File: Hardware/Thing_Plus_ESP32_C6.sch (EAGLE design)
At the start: 48 parts, among them J1 THING_PLUS_LOGICAL, J4 QWIIC_RIGHT_ANGLE, J5 MICRO-SDFRICTION, Q1 20V/4.2A/52mΩ/1.4W, U1 ESP32-C6-WROOM-1-NARROW, U2 RT9080-33GJ5, U3 MCP73831, U4 MAX17048

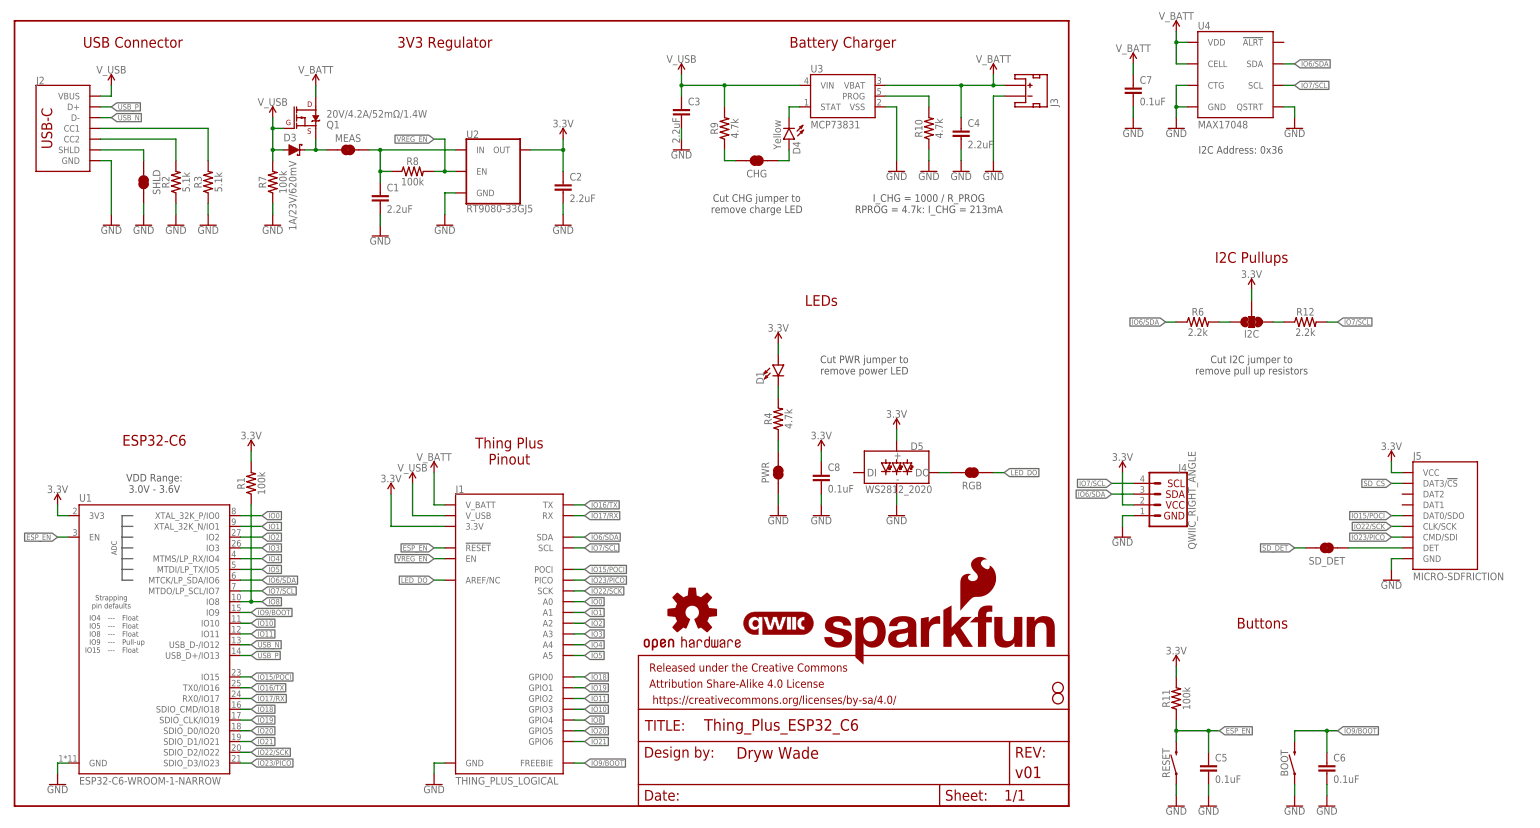
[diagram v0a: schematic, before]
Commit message: Finish initial schematic and layout
Organized schematic
Rearranged power circuitry to make routing other components easier
Finished routing board
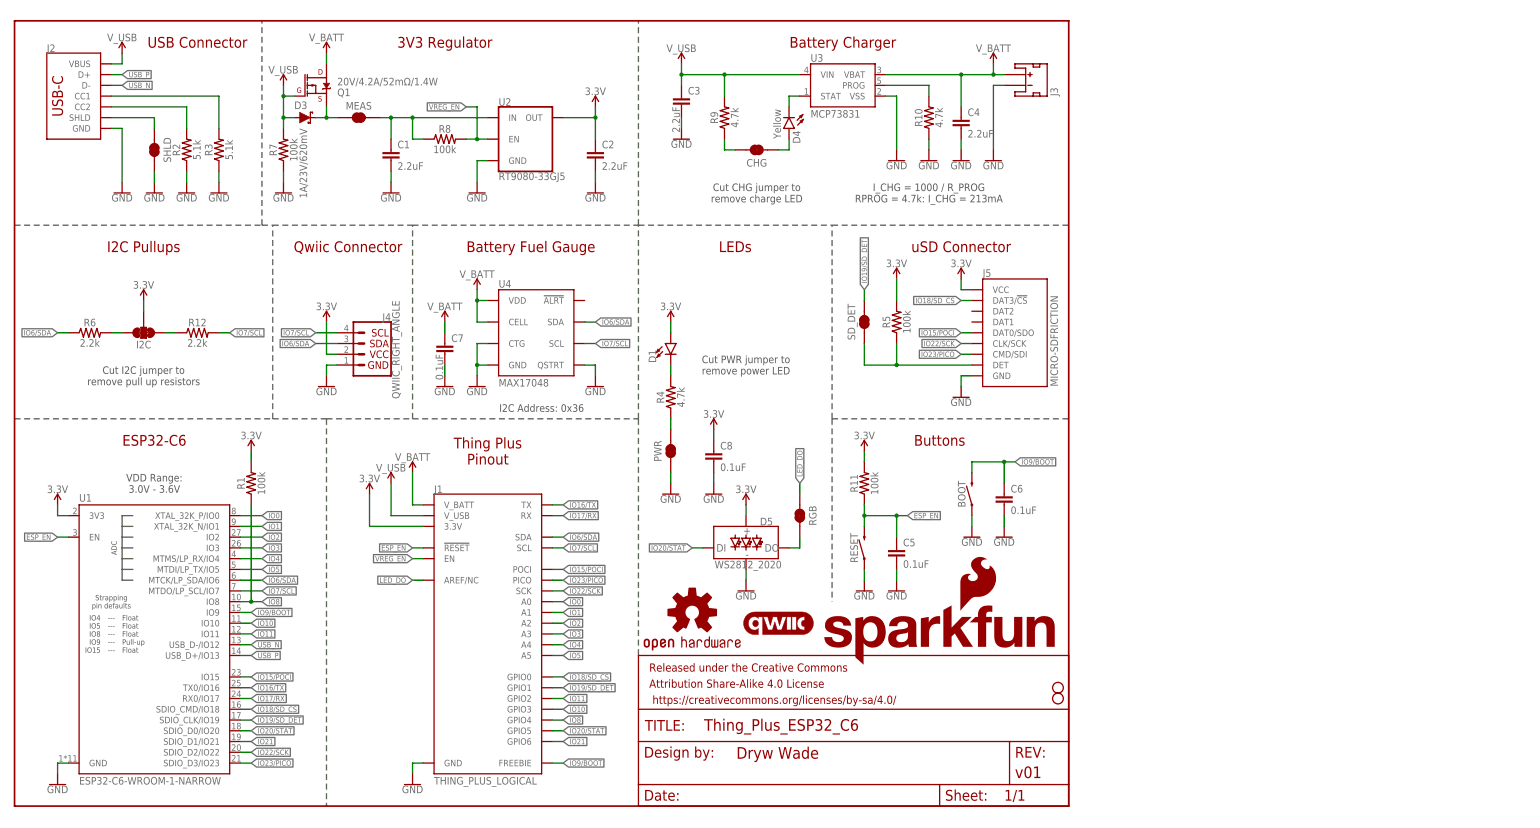
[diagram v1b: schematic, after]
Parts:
- added R5: 100k, SparkFun-Resistors:100KOHM-0603-1/10W-1%
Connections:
- removed net IO18: J1.GPIO0, U1.SDIO_CMD/IO18
- removed net IO19: J1.GPIO1, U1.SDIO_CLK/IO19
- removed net IO20: J1.GPIO5, U1.SDIO_D0/IO20
- removed net SD_CS: J5.DAT3/!CS!
- removed net SD_DET: SD_DET.2
- new net IO18/SD_CS: J1.GPIO0, J5.DAT3/!CS!, U1.SDIO_CMD/IO18
- new net IO19/SD_DET: J1.GPIO1, SD_DET.2, U1.SDIO_CLK/IO19
- new net IO20/STAT: D5.DI, J1.GPIO5, U1.SDIO_D0/IO20
- net 3.3V: now also R5.2
- net N$3: now also R5.1
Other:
- note added: "Battery Fuel Gauge"
- note added: "Qwiic Connector"
- note added: "uSD Connector"
- moved on the sheet: BOOT, C1, C2, C3, C4, C5, C6, C7, C8, CHG, D1, D3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

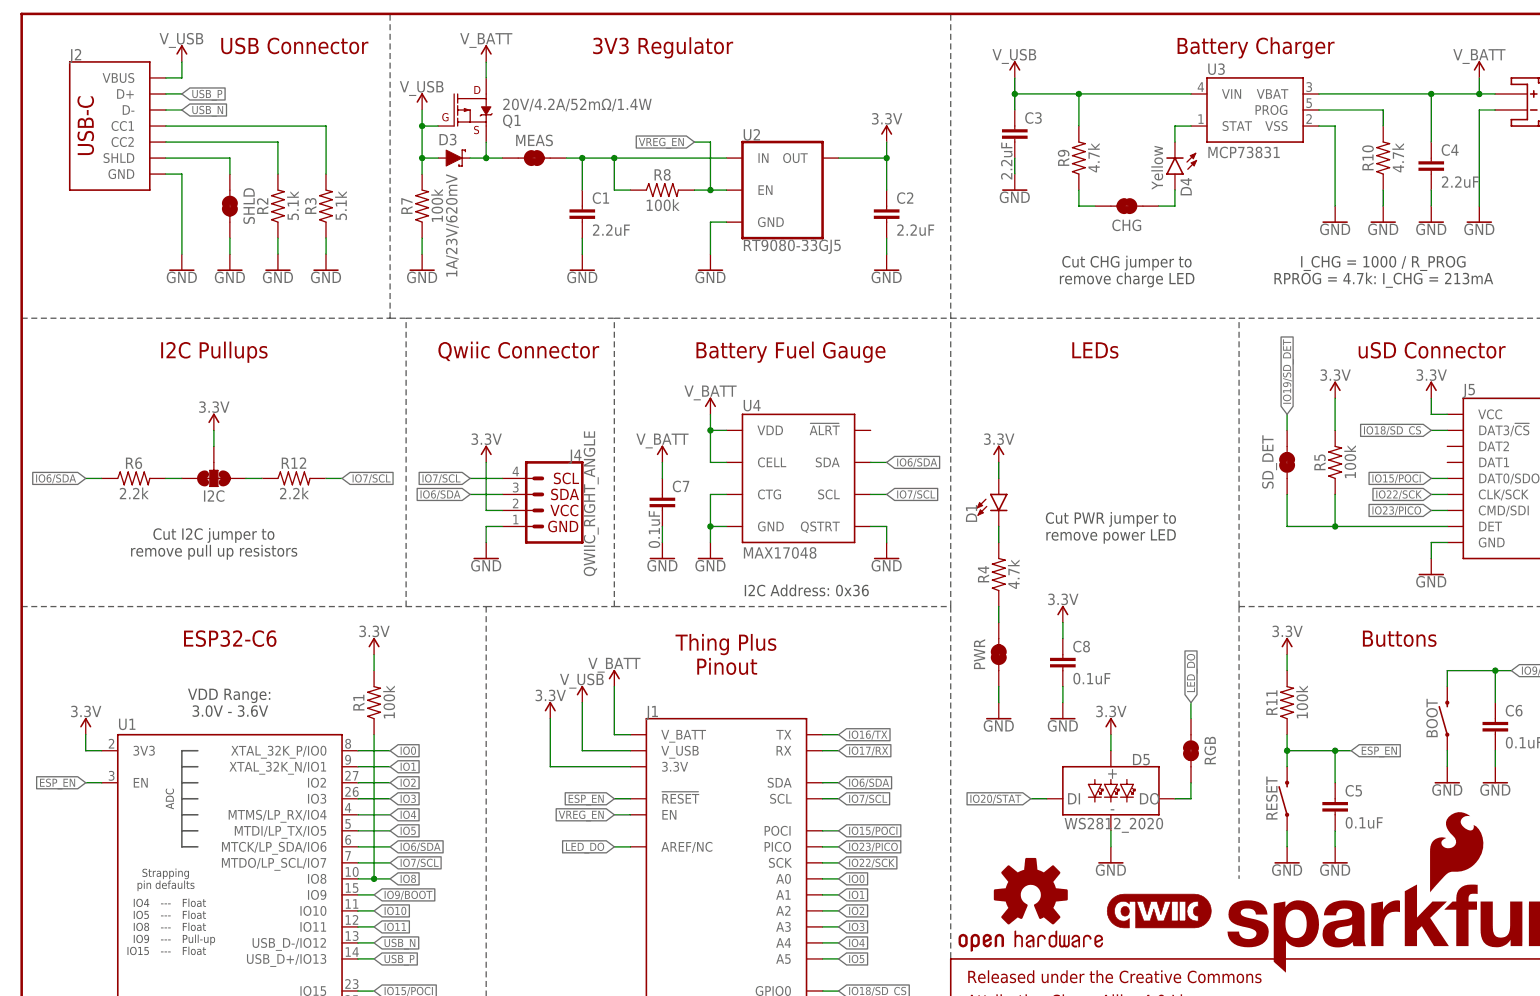
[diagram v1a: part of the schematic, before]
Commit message: Design review updates
Add measures
Add ordering instructions
Add notes about jumpers
Add voltage regulator parameters
Rearrange LED section in schematic
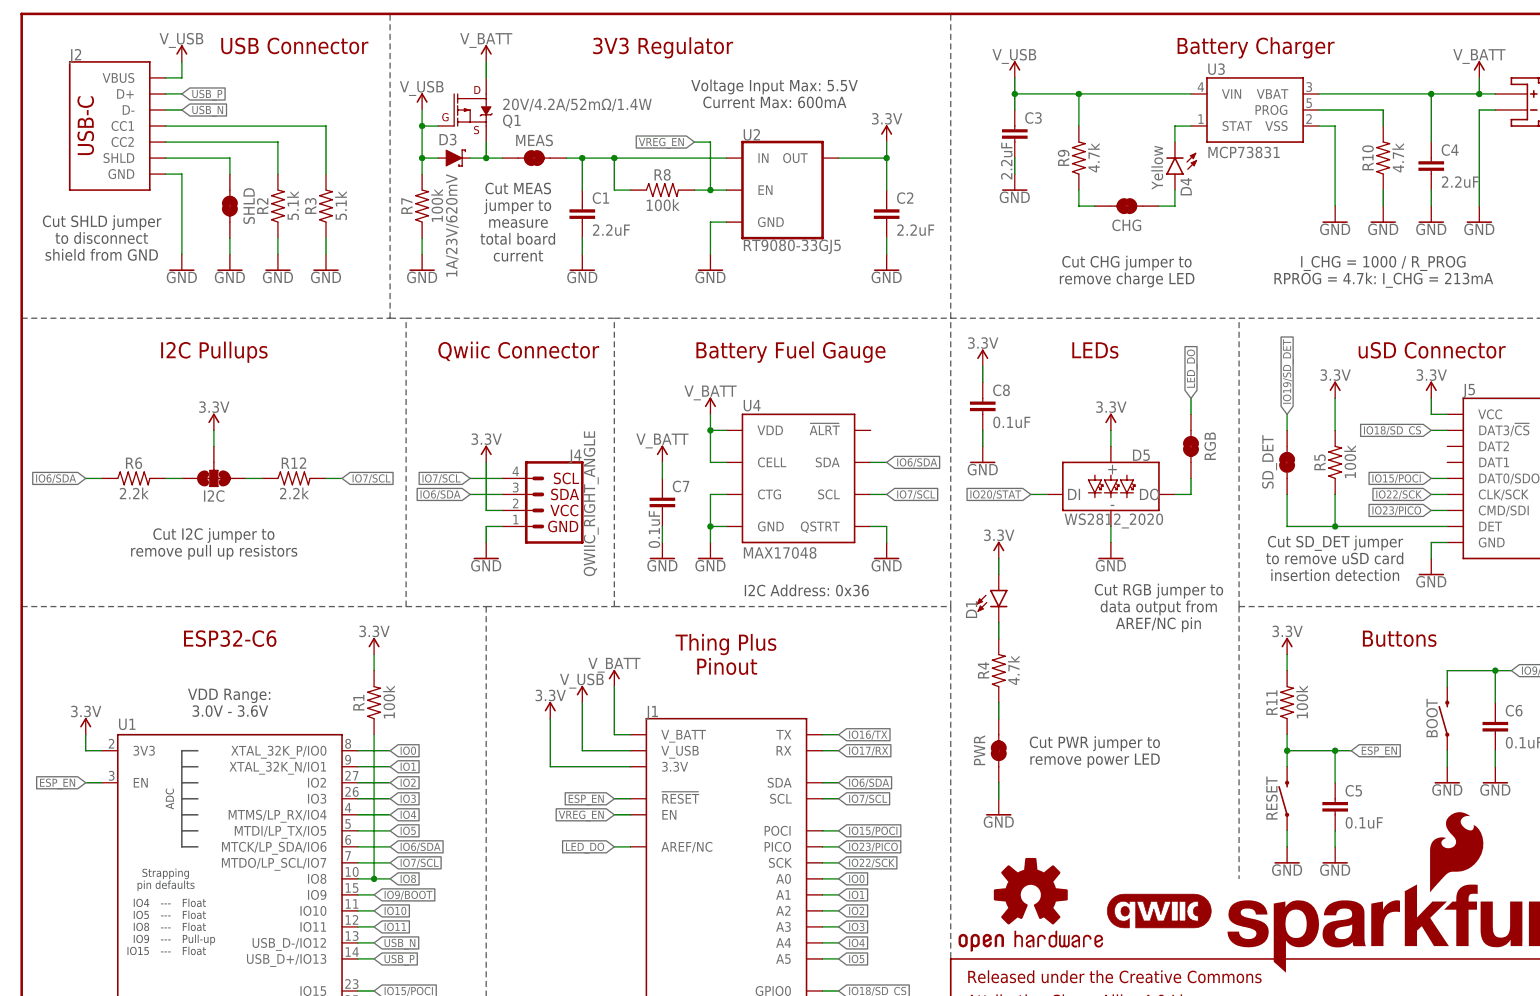
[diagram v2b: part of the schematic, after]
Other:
- note added: "Cut MEAS jumper to measure total board current"
- note added: "Cut RGB jumper to data output from AREF/NC pin"
- note added: "Cut SD_DET jumper to remove uSD card insertion detection"
- note added: "Cut SHLD jumper to disconnect shield from GND"
- note added: "Voltage Input Max: 5.5V Current Max: 600mA"
- moved on the sheet: C8, D1, D5, PWR, R4, RGB

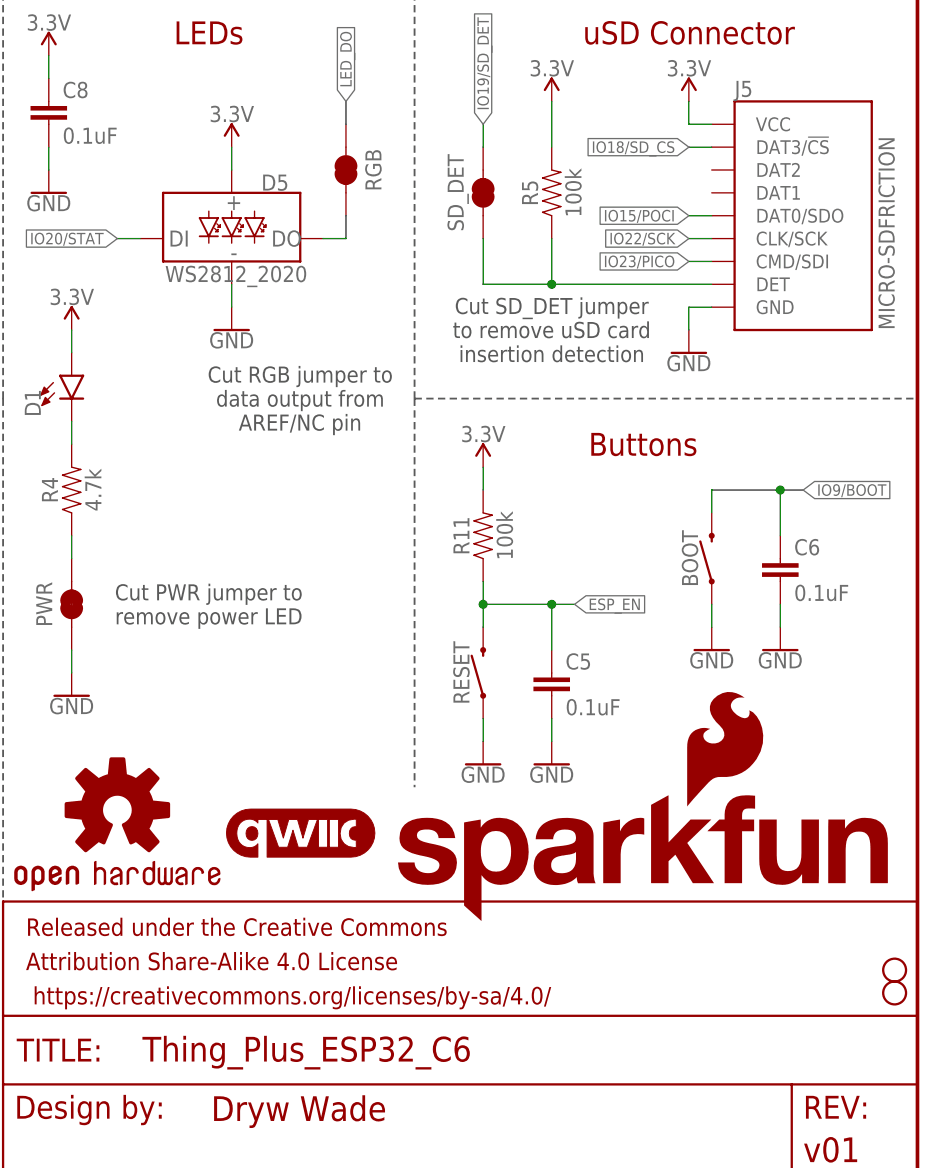
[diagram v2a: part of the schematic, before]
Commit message: Design review updates
Add fiducials
Add top mounting holes under ESP32-C6 antenna
Move OSHW logo and make bigger
Change RGB jumper to NO
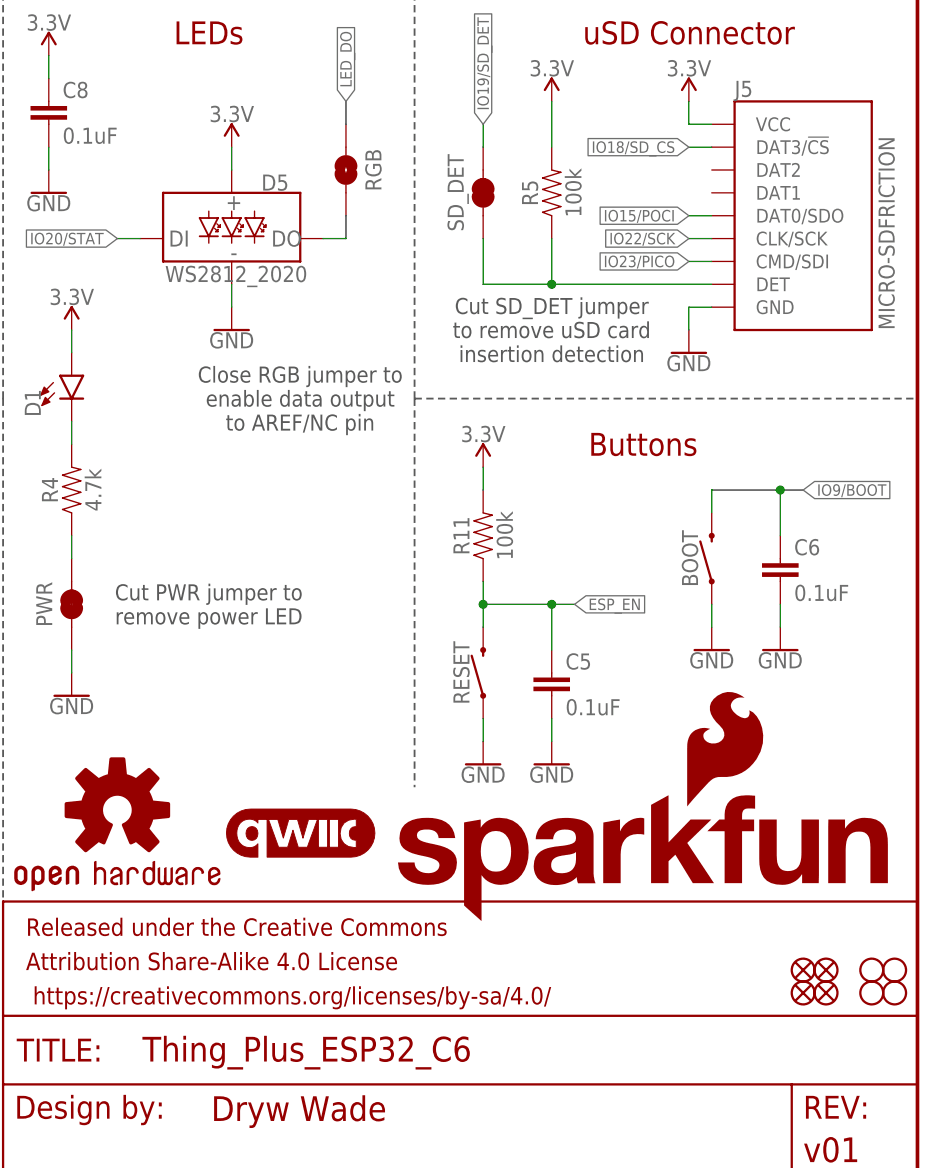
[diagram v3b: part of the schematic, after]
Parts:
- added FD1, FD2, FD3, FD4: FIDUCIALUFIDUCIAL, SparkFun-Aesthetics:FIDUCIALUFIDUCIAL
- added H3, H4: STAND-OFF, SparkFun-Hardware:STAND-OFF
- LOGO3: value OSHW-LOGOS -> OSHW-LOGOM; device SparkFun-Aesthetics:OSHW-LOGOS -> SparkFun-Aesthetics:OSHW-LOGOM
- RGB: value JUMPER-SMT_2_NC_TRACE_SILK -> JUMPER-SMT_2_NO_SILK; device SparkFun-Jumpers:JUMPER-SMT_2_NC_TRACE_SILK -> SparkFun-Jumpers:JUMPER-SMT_2_NO_SILK
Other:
- note added: "Close RGB jumper to enable data output to AREF/NC pin"
- note removed: "Cut RGB jumper to data output from AREF/NC pin"
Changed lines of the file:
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@@
 <part name="LOGO1" library="SparkFun-Aesthetics" deviceset="SFE_LOGO_NAME_FLAME" device=".1_INCH"/>
 <part name="LOGO2" library="SparkFun-Aesthetics" deviceset="QWIIC_LOGO" device="_4MM" value="QWIIC_LOGO_4MM"/>
-<part name="LOGO3" library="SparkFun-Aesthetics" deviceset="OSHW-LOGO" device="S"/>
+<part name="LOGO3" library="SparkFun-Aesthetics" deviceset="OSHW-LOGO" device="M" value="OSHW-LOGOM"/>
 <part name="SUPPLY1" library="SparkFun-PowerSymbols" deviceset="3.3V" device=""/>
 <part name="GND1" library="SparkFun-PowerSymbols" deviceset="GND" device=""/>
@@
 <part name="SD_DET" library="SparkFun-Jumpers" deviceset="JUMPER-SMT_2_NC_TRACE" device="_SILK" package3d_urn="urn:adsk.eagle:package:39281/1"/>
 <part name="MEAS" library="SparkFun-Jumpers" deviceset="JUMPER-COMBO_2_NC_TRACE" device=""/>
-<part name="RGB" library="SparkFun-Jumpers" deviceset="JUMPER-SMT_2_NC_TRACE" device="_SILK" package3d_urn="urn:adsk.eagle:package:39281/1"/>
+<part name="RGB" library="SparkFun-Jumpers" deviceset="JUMPER-SMT_2_NO" device="_SILK" package3d_urn="urn:adsk.eagle:package:39279/1"/>
 <part name="R5" library="SparkFun-Resistors" deviceset="100KOHM" device="-0603-1/10W-1%" value="100k"/>
 <part name="SUPPLY21" library="SparkFun-PowerSymbols" deviceset="3.3V" device=""/>
+<part name="H3" library="SparkFun-Hardware" deviceset="STAND-OFF" device=""/>
+<part name="H4" library="SparkFun-Hardware" deviceset="STAND-OFF" device=""/>
+<part name="FD1" library="SparkFun-Aesthetics" deviceset="FIDUCIAL" device="UFIDUCIAL" value="FIDUCIALUFIDUCIAL"/>
+<part name="FD2" library="SparkFun-Aesthetics" deviceset="FIDUCIAL" device="UFIDUCIAL" value="FIDUCIALUFIDUCIAL"/>
+<part name="FD3" library="SparkFun-Aesthetics" deviceset="FIDUCIAL" device="UFIDUCIAL" value="FIDUCIALUFIDUCIAL"/>
+<part name="FD4" library="SparkFun-Aesthetics" deviceset="FIDUCIAL" device="UFIDUCIAL" value="FIDUCIALUFIDUCIAL"/>
 </parts>
 <sheets>
@@
 to remove uSD card
 insertion detection</text>
-<text x="180.34" y="91.44" size="1.778" layer="97" font="vector" align="center">Cut RGB jumper to
-data output from
-AREF/NC pin</text>
+<text x="180.34" y="91.44" size="1.778" layer="97" font="vector" align="center">Close RGB jumper to
+enable data output
+to AREF/NC pin</text>
 </plain>
 <instances>
@@
 <attribute name="VALUE" x="208.28" y="127.254" size="1.778" layer="96" font="vector" align="bottom-center"/>
 </instance>
+<instance part="H3" gate="G$1" x="243.84" y="25.4" smashed="yes"/>
+<instance part="H4" gate="G$1" x="243.84" y="27.94" smashed="yes"/>
+<instance part="FD1" gate="G$1" x="238.76" y="25.4" smashed="yes"/>
+<instance part="FD2" gate="G$1" x="236.22" y="25.4" smashed="yes"/>
+<instance part="FD3" gate="G$1" x="236.22" y="27.94" smashed="yes"/>
+<instance part="FD4" gate="G$1" x="238.76" y="27.94" smashed="yes"/>
 </instances>
 <busses>
